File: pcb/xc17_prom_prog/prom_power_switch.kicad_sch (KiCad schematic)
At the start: 74 parts, among them Q1 BC850, Q10 BC850, Q11 IRLML9301, Q12 IRLML9301, Q13 IRLML9301, Q14 IRLML9301, Q15 BC850, Q16 IRLML9301, Q17 IRLML9301, Q18 IRLML9301, Q19 IRLML9301, Q2 BC850, Q20 BC850, Q21 BC850, Q22 BC850, Q23 BC850, Q24 BC850, Q3 IRLML9301, Q4 IRLML9301, Q5 IRLML9301, Q6 BC850, Q7 IRLML9301, Q8 IRLML9301, Q9 BC850

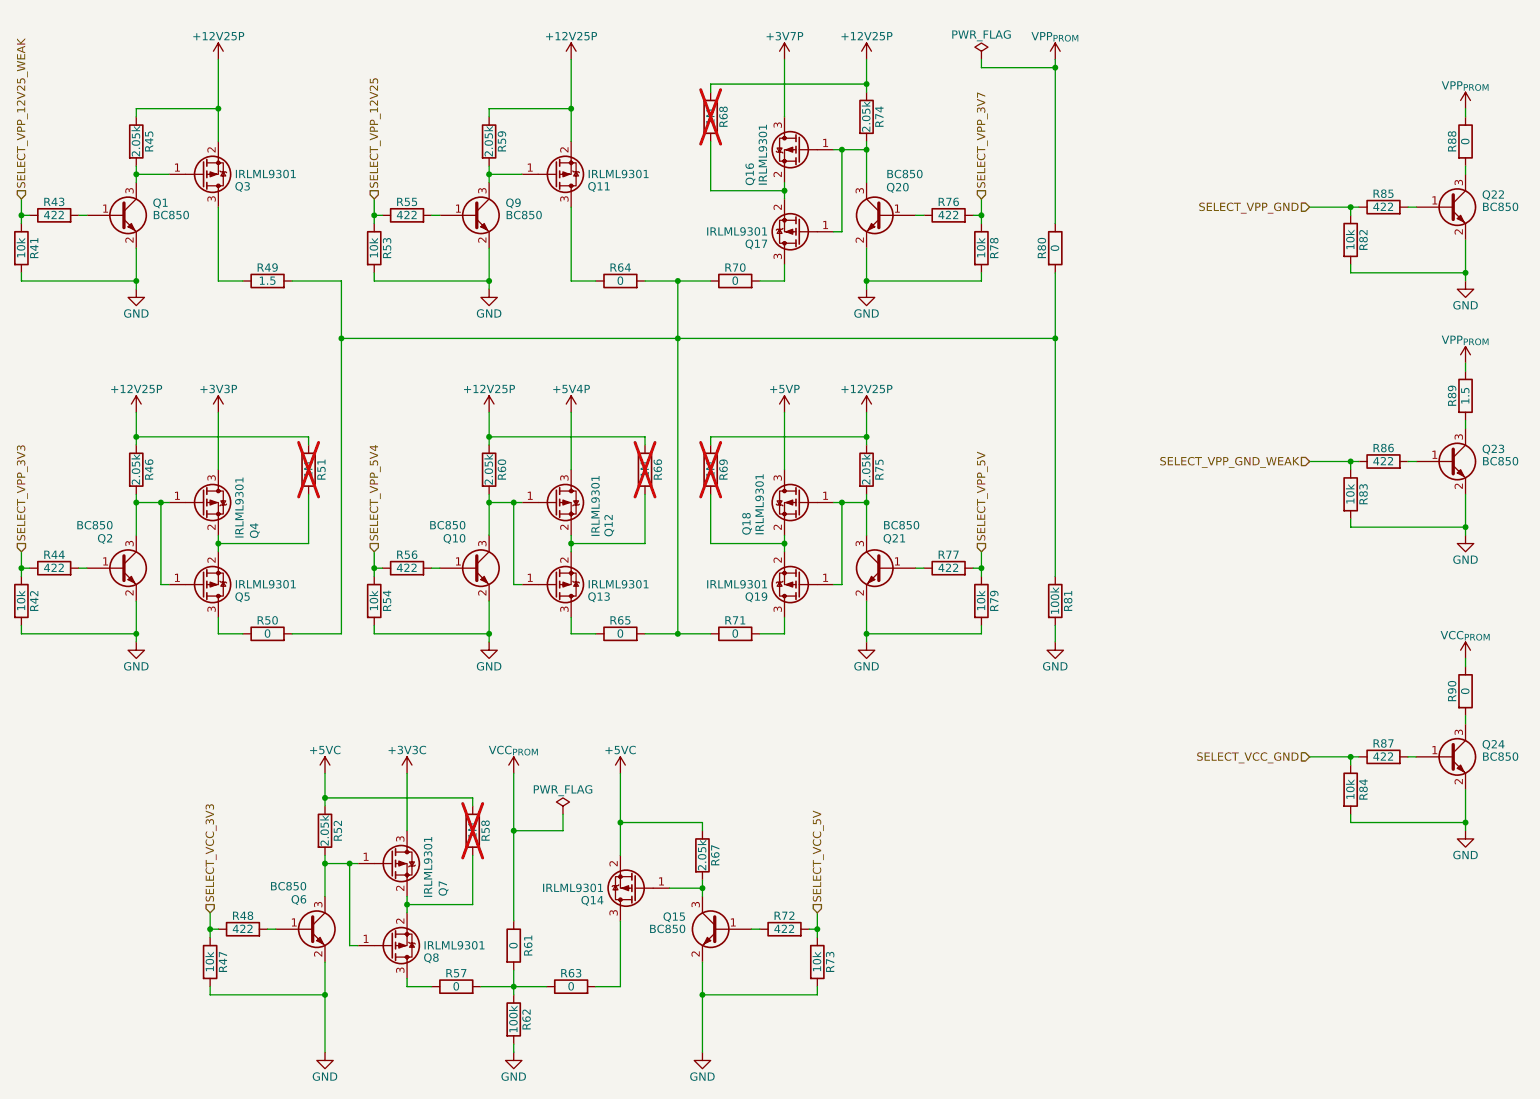
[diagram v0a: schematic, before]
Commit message: Fix voltage over-/under-shots
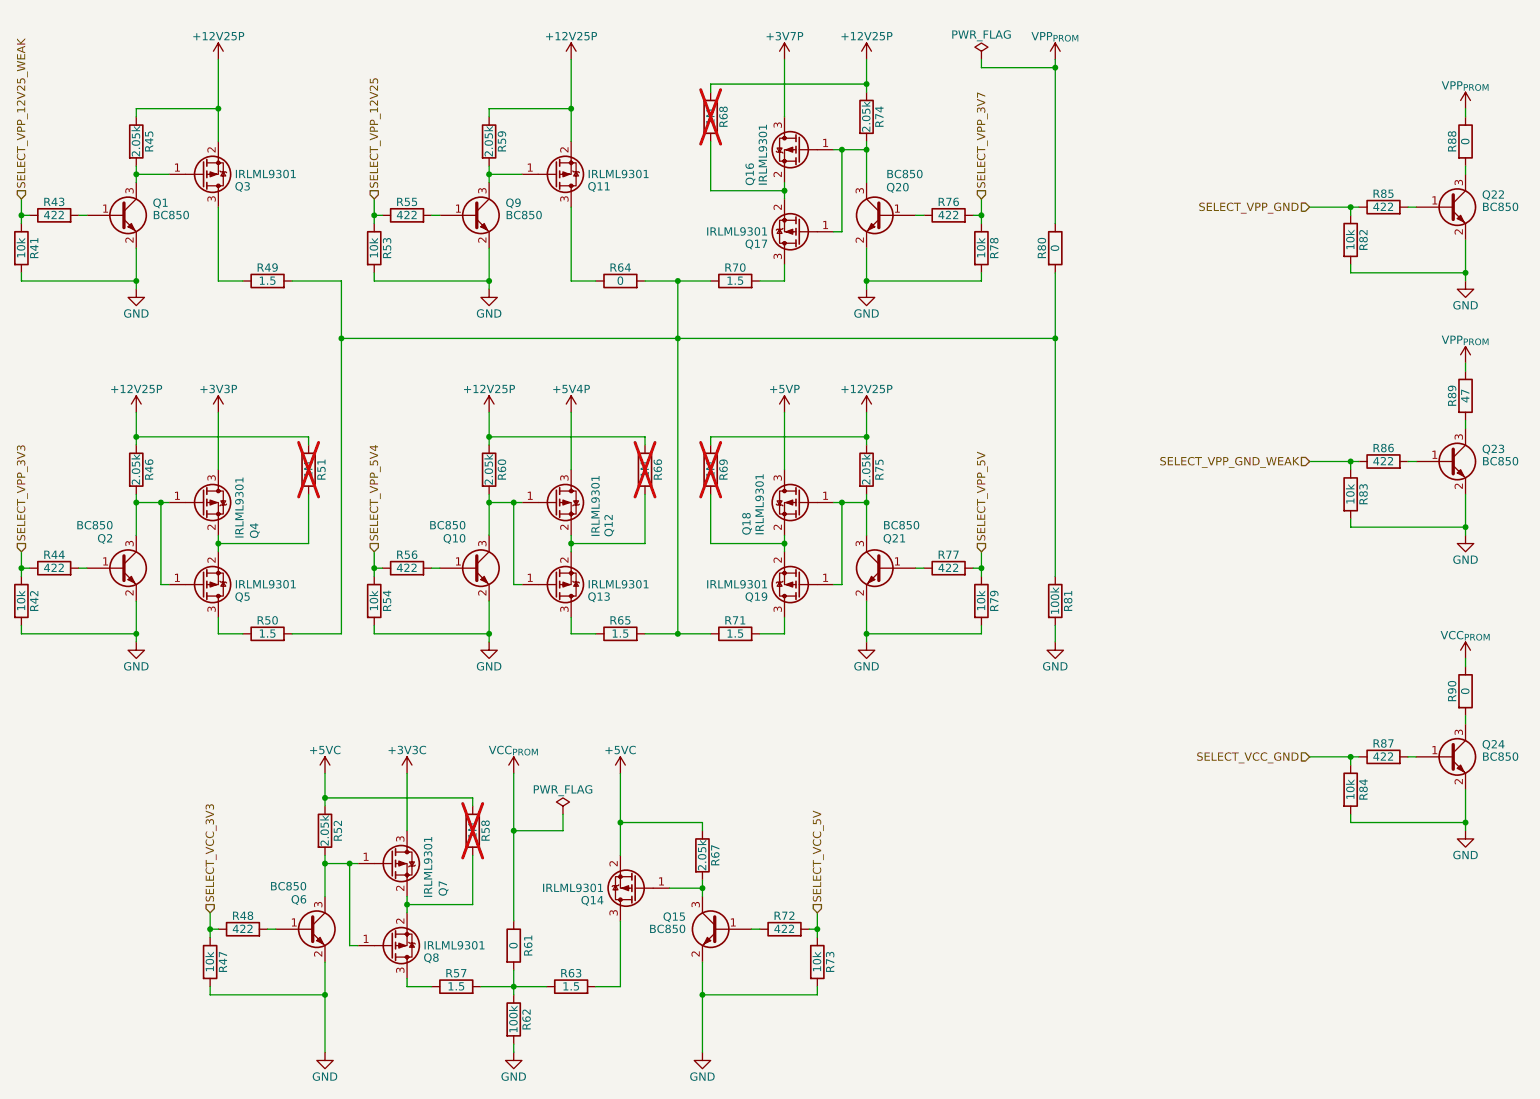
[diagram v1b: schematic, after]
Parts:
- R50, R57, R63, R65, R70, R71: value 0 -> 1.5
- R89: value 1.5 -> 47
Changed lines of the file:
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@@
 	(title_block
 		(title "XC17xxx PROM Programmer")
-		(date "2024-12-08")
+		(date "2024-12-29")
 		(rev "2")
 		(company "CC-BY-SA-4.0 Michael Singer")
@@
 			)
 		)
-		(property "Value" "0"
+		(property "Value" "1.5"
 			(at 107.95 170.18 90)
 			(effects
@@
 			)
 		)
-		(property "Value" "0"
+		(property "Value" "1.5"
 			(at 133.35 60.96 90)
 			(effects
@@
 			)
 		)
-		(property "Value" "0"
+		(property "Value" "1.5"
 			(at 133.35 115.57 90)
 			(effects
@@
 			)
 		)
-		(property "Value" "0"
+		(property "Value" "1.5"
 			(at 60.96 115.57 90)
 			(effects
@@
 			)
 		)
-		(property "Value" "0"
+		(property "Value" "1.5"
 			(at 115.57 115.57 90)
 			(effects
@@
 			)
 		)
-		(property "Value" "0"
+		(property "Value" "1.5"
 			(at 90.17 170.18 90)
 			(effects
@@
 			)
 		)
-		(property "Value" "1.5"
+		(property "Value" "47"
 			(at 246.38 78.74 90)
 			(effects

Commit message: Remove unused components
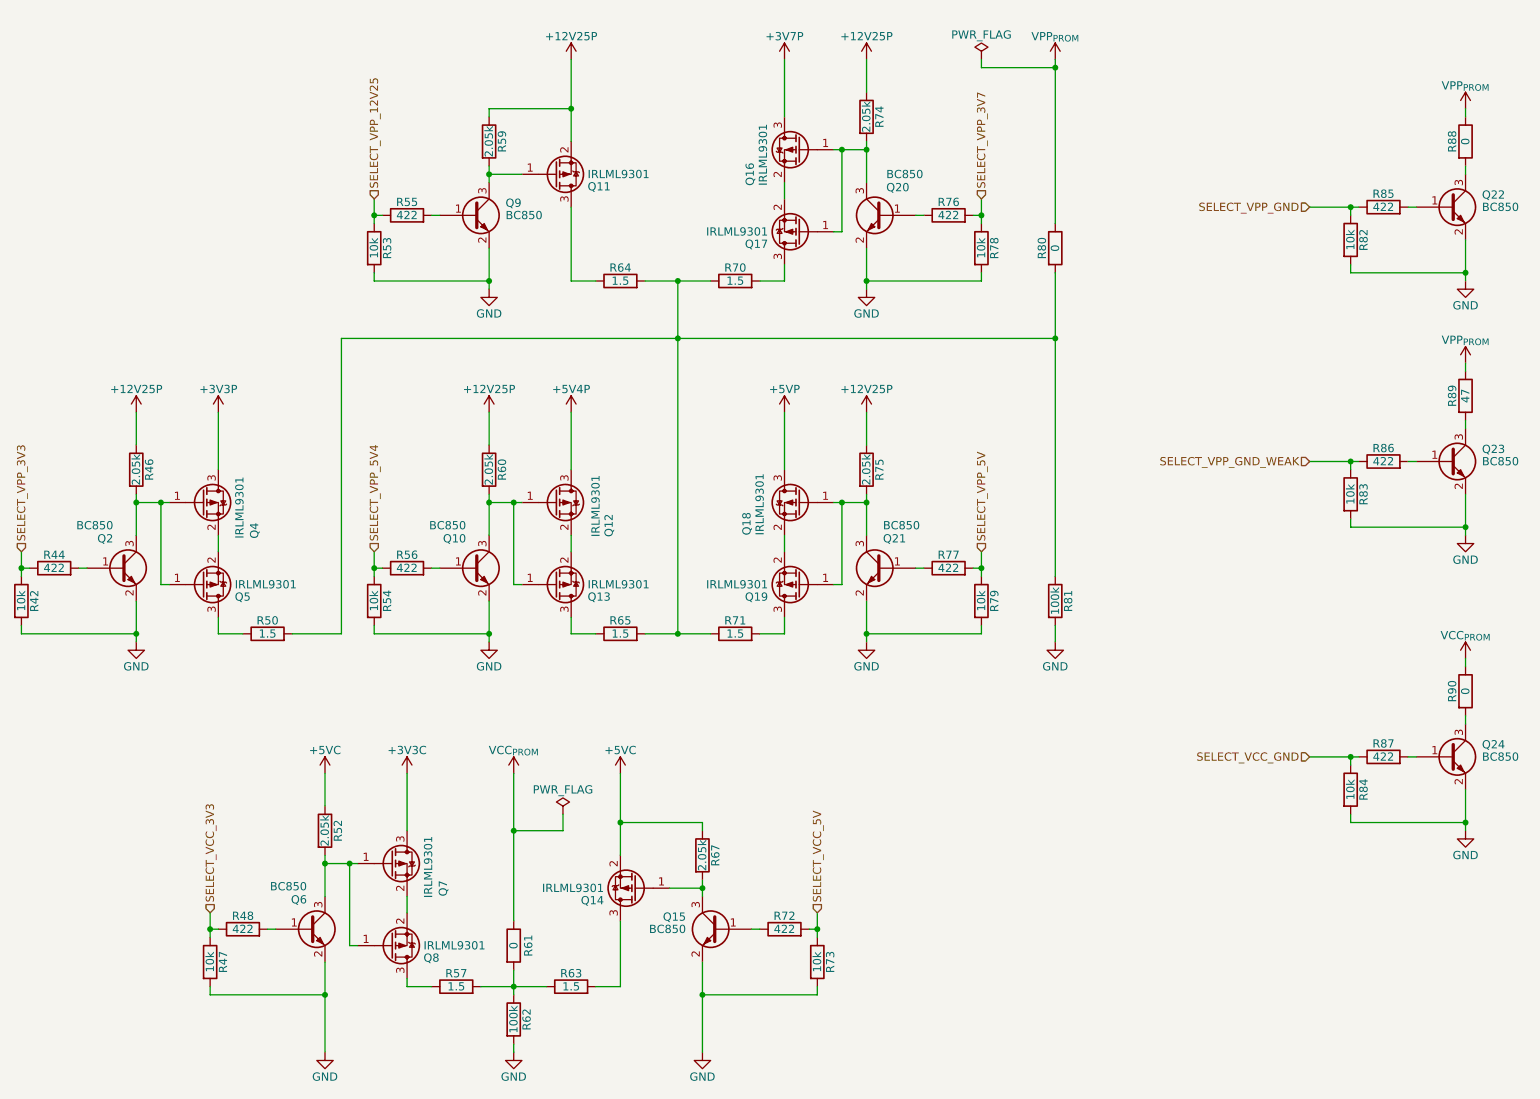
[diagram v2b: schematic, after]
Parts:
- removed Q1: BC850, Package_TO_SOT_SMD:SOT-23, symbol Transistor_BJT:BC850
- removed Q3: IRLML9301, Package_TO_SOT_SMD:SOT-23, symbol Transistor_FET:IRLML9301
- removed R41: 10k, Resistor_SMD:R_0603_1608Metric, symbol Device:R
- removed R43: 422, Resistor_SMD:R_0603_1608Metric, symbol Device:R
- removed R45: 2.05k, Resistor_SMD:R_0603_1608Metric, symbol Device:R
- removed R49: 1.5, Resistor_SMD:R_0603_1608Metric, symbol Device:R
- removed R51, R58, R66, R68, R69: 1M, Resistor_SMD:R_0603_1608Metric, symbol Device:R
- R64: value 0 -> 1.5

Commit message: Migrate from HX1K to HX4K FPGA
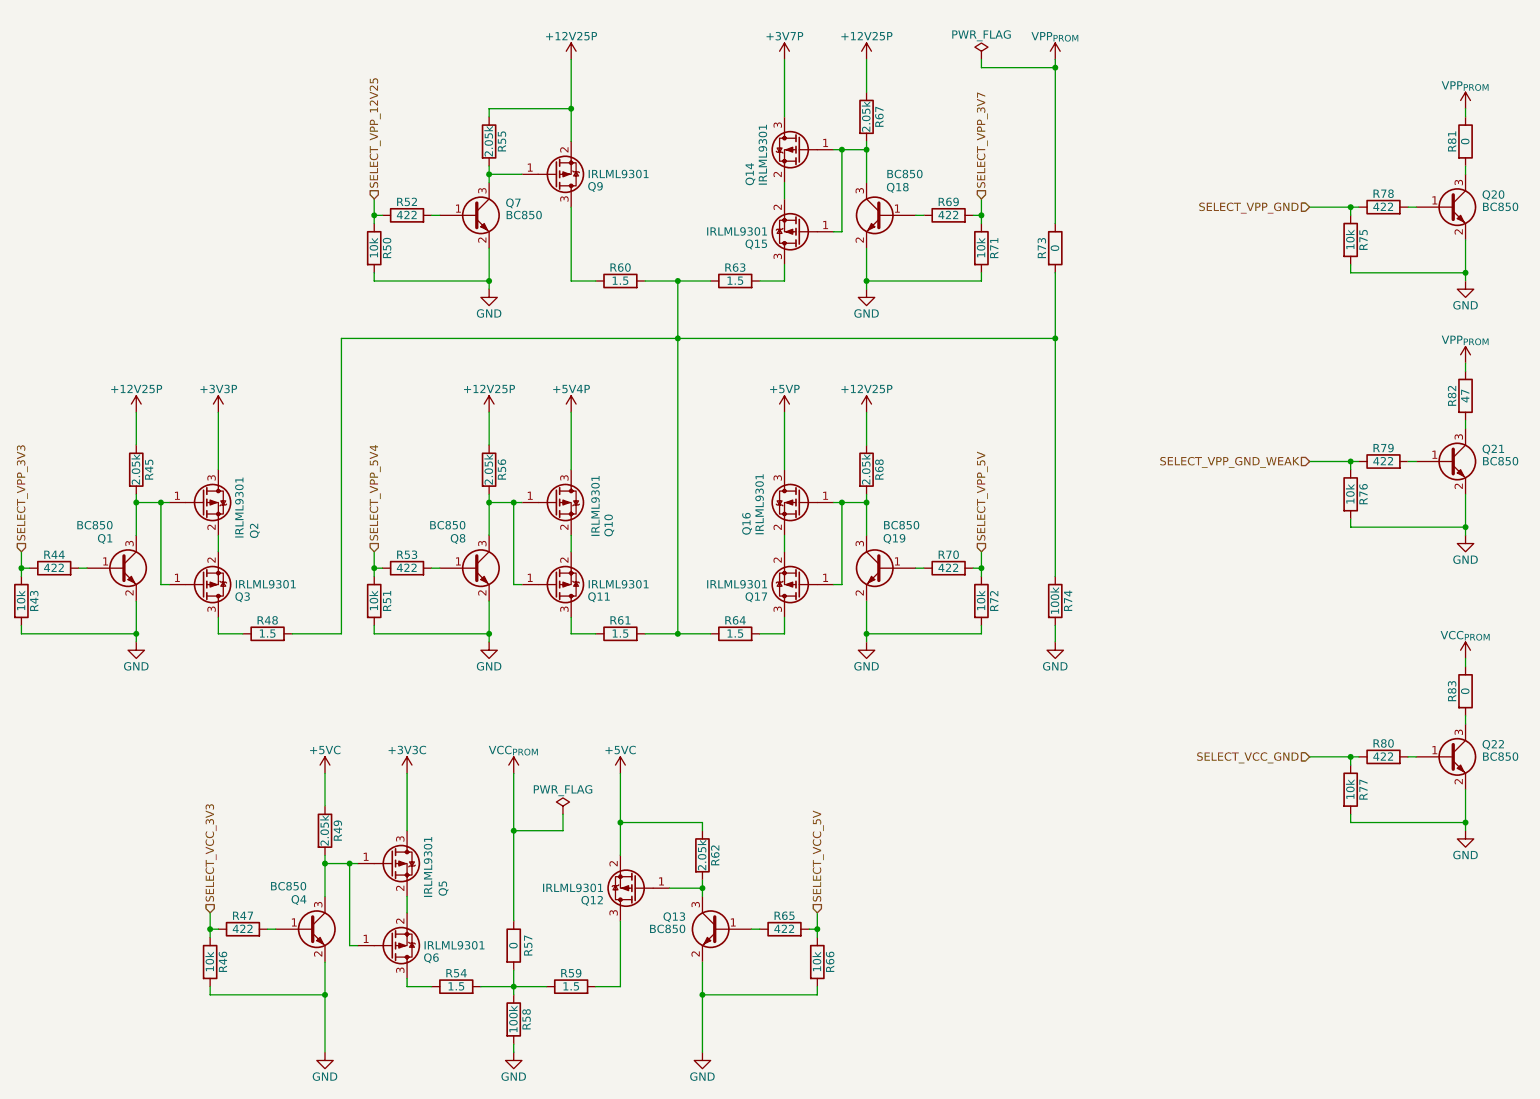
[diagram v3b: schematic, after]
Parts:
- renumbered Q2 to Q1, Q12 to Q10, Q13 to Q11, Q14 to Q12, Q15 to Q13, Q16 to Q14, Q17 to Q15, Q18 to Q16, Q19 to Q17, Q20 to Q18, Q21 to Q19, Q4 to Q2, Q22 to Q20, Q23 to Q21, Q24 to Q22, Q5 to Q3, Q6 to Q4, Q7 to Q5, Q8 to Q6, Q9 to Q7, Q10 to Q8, Q11 to Q9, R42 to R43, R46 to R45, R47 to R46, R48 to R47, R50 to R48, R52 to R49, R53 to R50, R54 to R51, R55 to R52, R56 to R53, R57 to R54, R59 to R55, R60 to R56, R61 to R57, R62 to R58, R63 to R59, R64 to R60, R65 to R61, R67 to R62, R70 to R63, R71 to R64, R72 to R65, R73 to R66, R74 to R67, R75 to R68, R76 to R69, R77 to R70, R78 to R71, R79 to R72, R80 to R73, R81 to R74, R82 to R75, R83 to R76, R84 to R77, R85 to R78, R86 to R79, R87 to R80, R88 to R81, R89 to R82, R90 to R83
